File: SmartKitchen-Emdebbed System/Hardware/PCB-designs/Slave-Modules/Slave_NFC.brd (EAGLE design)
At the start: 90 x 80 mm, 29 parts, among them IC1 PCF8574T, IC2 7805DT, IC3 PCF8574T, IC4 74AHC1G126DBV, J1 RJ11-2L-B, J2 RJ11-2L-B, Q1 SPB80P06P, Q2 SPB80P06P, Q3 SPB80P06P

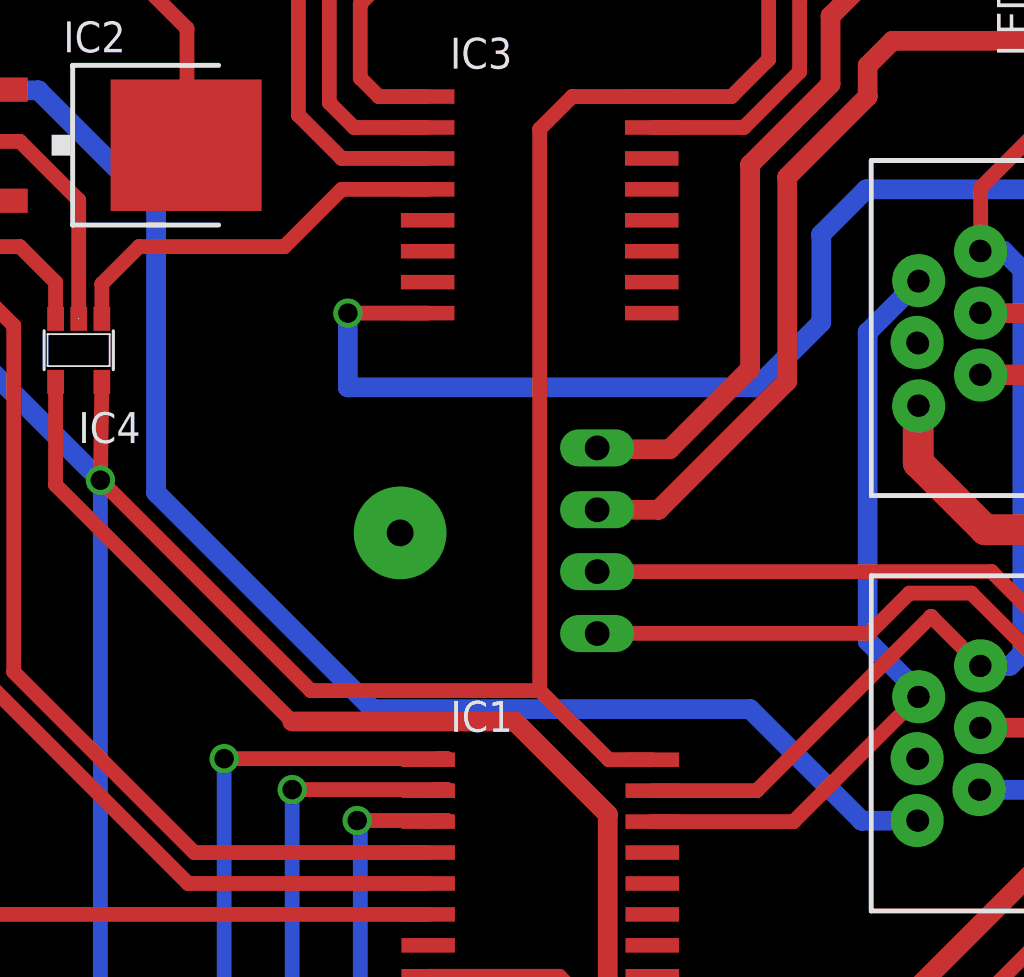
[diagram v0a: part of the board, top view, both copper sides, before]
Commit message: Testsoftware + Fix problem wire
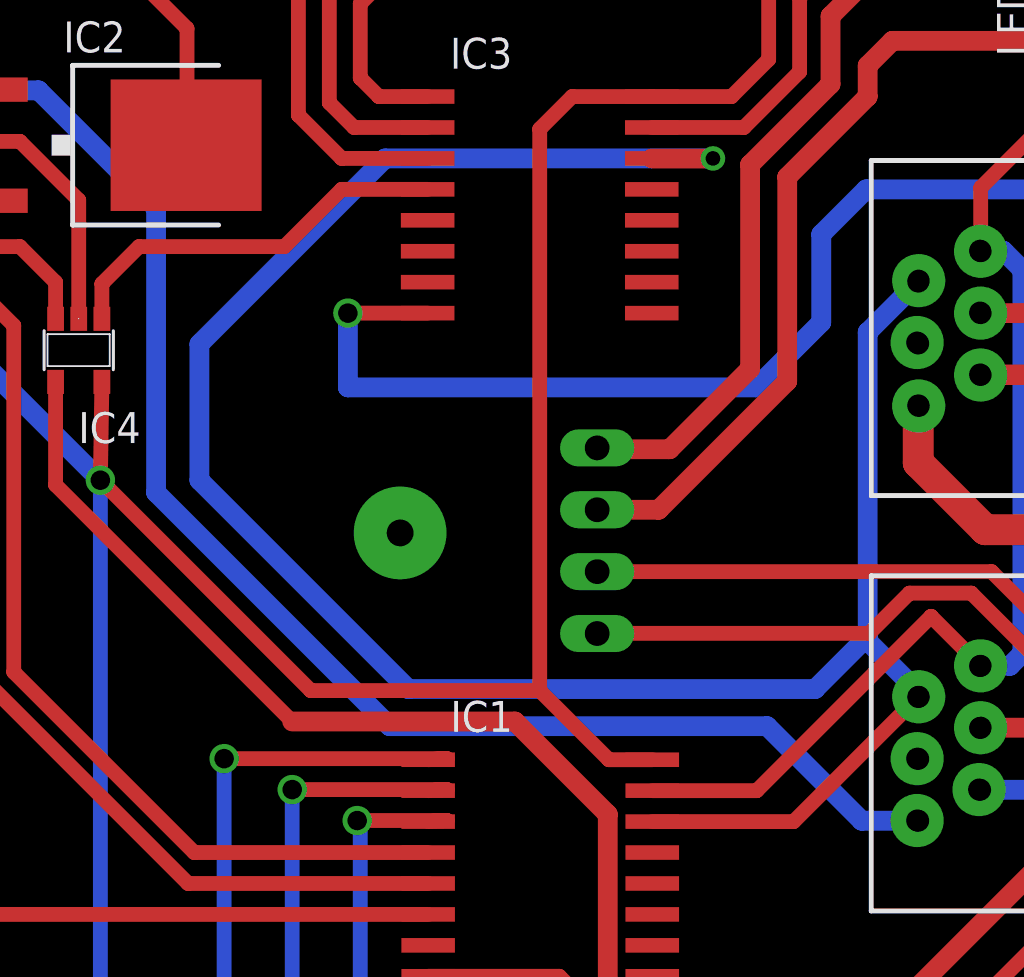
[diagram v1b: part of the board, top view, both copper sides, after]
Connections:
- net N$3: now also IC3.14
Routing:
- net N$3: track 31.8 -> 96.0 mm, vias 0 -> 1
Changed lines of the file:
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@@
 <wire x1="66.523" y1="76.225" x2="66.548" y2="76.2" width="1.27" layer="16"/>
 <wire x1="74.72" y1="28.185" x2="72.399" y2="28.185" width="0.8128" layer="16"/>
-<wire x1="72.399" y1="28.185" x2="67.818" y2="32.766" width="0.8128" layer="16"/>
-<wire x1="67.818" y1="32.766" x2="52.324" y2="32.766" width="0.8128" layer="16"/>
-<wire x1="52.324" y1="32.766" x2="43.434" y2="41.656" width="0.8128" layer="16"/>
+<wire x1="53.0225" y1="32.0675" x2="43.434" y2="41.656" width="0.8128" layer="16"/>
 <wire x1="43.434" y1="41.656" x2="43.434" y2="53.34" width="0.8128" layer="16"/>
 <wire x1="43.434" y1="53.34" x2="38.608" y2="58.166" width="0.8128" layer="16"/>
 <wire x1="38.608" y1="58.166" x2="35.306" y2="58.166" width="0.8128" layer="16"/>
 <wire x1="35.335" y1="58.195" x2="37.3675" y2="58.195" width="0.6096" layer="1"/>
+<wire x1="53.0225" y1="32.0675" x2="68.5165" y2="32.0675" width="0.8128" layer="16"/>
+<wire x1="68.5165" y1="32.0675" x2="72.399" y2="28.185" width="0.8128" layer="16"/>
 </signal>
 <signal name="N$1">
@@
 <wire x1="74.72" y1="33.265" x2="74.72" y2="33.484" width="0.8128" layer="16"/>
 <wire x1="74.72" y1="33.484" x2="72.644" y2="35.56" width="0.8128" layer="16"/>
-<wire x1="72.644" y1="35.56" x2="72.644" y2="48.239" width="0.8128" layer="16"/>
+<wire x1="72.644" y1="35.56" x2="72.644" y2="35.7505" width="0.8128" layer="16"/>
 <wire x1="72.644" y1="48.239" x2="74.72" y2="50.315" width="0.8128" layer="16"/>
 <wire x1="63.8025" y1="28.15" x2="69.605" y2="28.15" width="0.6096" layer="1"/>
 <wire x1="69.605" y1="28.15" x2="74.72" y2="33.265" width="0.6096" layer="1"/>
+<contactref element="IC3" pad="14"/>
+<wire x1="72.644" y1="48.239" x2="72.644" y2="35.7505" width="0.8128" layer="16"/>
+<wire x1="72.644" y1="35.7505" x2="70.485" y2="33.5915" width="0.8128" layer="16"/>
+<wire x1="70.485" y1="33.5915" x2="53.7845" y2="33.5915" width="0.8128" layer="16"/>
+<wire x1="53.7845" y1="33.5915" x2="45.212" y2="42.164" width="0.8128" layer="16"/>
+<wire x1="45.212" y1="42.164" x2="45.212" y2="47.752" width="0.8128" layer="16"/>
+<wire x1="45.212" y1="47.752" x2="52.832" y2="55.372" width="0.8128" layer="16"/>
+<wire x1="52.832" y1="55.372" x2="66.294" y2="55.372" width="0.8128" layer="16"/>
+<via x="66.294" y="55.372" extent="1-16" drill="0.6" shape="square"/>
+<wire x1="66.294" y1="55.372" x2="63.782" y2="55.372" width="0.8128" layer="1"/>
 </signal>
 <signal name="N$21">

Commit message: Optimized PCB-board 2.0 with header for MAX232
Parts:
- added X1: 22-23-2101, con-molex:22-23-2101
- moved INDILED 10.0 mm to (71.5, 39.7)
- moved R6 10.0 mm to (39.5, 24.3)
- moved IC1 10.0 mm to (69.2, 26.2)
- moved IC2 10.0 mm to (52.2, 55.9)
- moved IC3 10.0 mm to (69.2, 53.5)
- moved IC4 10.0 mm to (50.3, 47.5)
- moved J1 10.0 mm to (93.6, 48.4)
- moved J2 10.0 mm to (93.6, 31.4)
- moved LED1 10.0 mm to (91.0, 18.4)
- moved LED2 10.0 mm to (91.5, 61.5)
- moved Q1 10.0 mm to (28.6, 51.1)
- moved Q2 10.0 mm to (28.6, 37.7)
- moved Q3 10.0 mm to (28.6, 24.2)
- moved R1 10.0 mm to (43.7, 50.5)
- moved R10 10.0 mm to (82.6, 69.8)
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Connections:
- removed net N$27: IC4.2, SV1.5
- new net N$26: IC4.2, X1.2
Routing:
- net N$26: track 0.00 -> 91.0 mm, vias 0 -> 1
- net N$27: track 44.9 -> 0.00 mm
- net N$7: track 200.6 -> 231.9 mm
- net N$8: track 225.7 -> 222.5 mm
- net N$9: track 202.0 -> 200.5 mm
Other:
- board size 90 x 80 mm -> 100 x 80 mm
- board text added: "OAMK Design by Tom Mampaey Made in Finland"
- board text added: "Smart Fridge - OAMK"

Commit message: Adding interference capacitors and testingcode
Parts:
- added C1, C2: 100nF, rcl:C0603
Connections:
- net AGND: now also C1.1, C2.1
- net N$21: now also C1.2, C2.2
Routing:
- net AGND: track 311.1 -> 331.6 mm, vias 6 -> 7
- net N$21: track 224.4 -> 230.0 mm
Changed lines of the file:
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@@
 <setting verticaltext="up"/>
 </settings>
-<grid distance="0.02" unitdist="inch" unit="inch" style="lines" multiple="1" display="yes" altdistance="0.05" altunitdist="inch" altunit="inch"/>
+<grid distance="0.01" unitdist="inch" unit="inch" style="lines" multiple="1" display="yes" altdistance="0.05" altunitdist="inch" altunit="inch"/>
 <layers>
 <layer number="1" name="Top" color="4" fill="1" visible="yes" active="yes"/>
@@
 <attribute name="OC_FARNELL" value="1756828" x="11.2827" y="39.3733" size="1.778" layer="27" rot="R90" display="off"/>
 </element>
+<element name="C1" library="rcl" package="C0603" value="100nF" x="76.2" y="60.452" rot="R270"/>
+<element name="C2" library="rcl" package="C0603" value="100nF" x="76.2" y="33.02" rot="R270"/>
 </elements>
 <signals>
@@
 <via x="90.518" y="46.482" extent="1-16" drill="0.8" shape="square"/>
 <wire x1="90.518" y1="46.482" x2="87.283" y2="46.482" width="0.8128" layer="1"/>
-<wire x1="87.26" y1="29.455" x2="90.509" y2="29.455" width="0.8128" layer="16"/>
+<wire x1="87.26" y1="29.455" x2="89.154" y2="29.455" width="0.8128" layer="16"/>
+<wire x1="89.154" y1="29.455" x2="90.509" y2="29.455" width="0.8128" layer="16"/>
 <wire x1="90.509" y1="29.455" x2="90.518" y2="29.464" width="0.8128" layer="16"/>
 <wire x1="90.495" y1="46.505" x2="90.518" y2="46.482" width="0.8128" layer="16"/>
@@
 <via x="43.274" y="51.7525" extent="1-16" drill="0.6" shape="square"/>
 <wire x1="64.582" y1="49.022" x2="61.308" y2="49.022" width="0.6096" layer="1"/>
+<contactref element="C1" pad="1"/>
+<contactref element="C2" pad="1"/>
+<wire x1="76.2" y1="33.87" x2="77.47" y2="33.87" width="0.6096" layer="1"/>
+<wire x1="77.47" y1="33.87" x2="77.47" y2="30.734" width="0.6096" layer="1"/>
+<via x="77.47" y="30.734" extent="1-16" drill="0.6" shape="square"/>
+<wire x1="77.47" y1="30.734" x2="77.724" y2="30.48" width="0.6096" layer="16"/>
+<wire x1="77.724" y1="30.48" x2="78.232" y2="30.48" width="0.6096" layer="16"/>
+<wire x1="78.232" y1="30.48" x2="83.566" y2="25.146" width="0.6096" layer="16"/>
+<wire x1="83.566" y1="25.146" x2="85.344" y2="25.146" width="0.6096" layer="16"/>
+<wire x1="85.344" y1="25.146" x2="89.154" y2="28.956" width="0.6096" layer="16"/>
+<wire x1="89.154" y1="28.956" x2="89.154" y2="29.455" width="0.6096" layer="16"/>
 </signal>
 <signal name="N$4">
@@
 <wire x1="78.58" y1="62.484" x2="78.58" y2="59.436" width="0.6096" layer="1"/>
 <wire x1="78.58" y1="59.436" x2="77.056" y2="57.912" width="0.6096" layer="1"/>
-<wire x1="77.056" y1="57.912" x2="73.782" y2="57.912" width="0.6096" layer="1"/>
+<wire x1="77.056" y1="57.912" x2="76.2" y2="57.912" width="0.6096" layer="1"/>
+<wire x1="76.2" y1="57.912" x2="73.782" y2="57.912" width="0.6096" layer="1"/>
 <wire x1="95.4583" y1="5.715" x2="95.4583" y2="8.255" width="0.8128" layer="1"/>
 <wire x1="95.4583" y1="8.255" x2="95.4583" y2="10.795" width="0.8128" layer="1"/>
@@
 <wire x1="70.5155" y1="57.912" x2="69.182" y2="56.5785" width="0.6096" layer="1"/>
 <wire x1="69.182" y1="56.5785" x2="69.182" y2="33.528" width="0.6096" layer="1"/>
+<contactref element="C1" pad="2"/>
+<wire x1="76.2" y1="59.602" x2="76.2" y2="57.912" width="0.4064" layer="1"/>
+<contactref element="C2" pad="2"/>
+<wire x1="76.2" y1="32.17" x2="76.2" y2="30.734" width="0.6096" layer="1"/>
+<wire x1="76.2" y1="30.734" x2="73.8025" y2="30.734" width="0.6096" layer="1"/>
+<wire x1="73.8025" y1="30.734" x2="73.8025" y2="30.69" width="0.6096" layer="1"/>
 <wire x1="51.2115" y1="46.2005" x2="51.209" y2="46.198" width="0" layer="19" extent="1-1"/>
 </signal>

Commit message: Final PCB-design for NFC-reader modules
I'm proud
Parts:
- added C3, C4: 100n, resistor:C0603
- C1, C2: value 100nF -> 4µ7; device rcl:C0603 -> resistor:PANASONIC_B
- moved C1 36.7 mm to (79.2, 23.9), turned to 0 degrees
- moved C2 8.68 mm to (79.2, 41.1), turned to 0 degrees
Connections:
- net AGND: now also C1.-, C2.-, C3.1, C4.1; no longer C1.1, C2.1
- net N$10: now also C1.+, C2.+, J1.3, J2.3
- net N$21: now also C3.2, C4.2; no longer C1.2, C2.2
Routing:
- net AGND: track 331.6 -> 311.1 mm, vias 7 -> 27
- net N$10: track 338.7 -> 356.7 mm
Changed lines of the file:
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@@
 <setting verticaltext="up"/>
 </settings>
-<grid distance="0.01" unitdist="inch" unit="inch" style="lines" multiple="1" display="yes" altdistance="0.05" altunitdist="inch" altunit="inch"/>
+<grid distance="0.00125" unitdist="inch" unit="inch" style="lines" multiple="1" display="yes" altdistance="0.05" altunitdist="inch" altunit="inch"/>
 <layers>
 <layer number="1" name="Top" color="4" fill="1" visible="yes" active="yes"/>
@@
 <wire x1="80" y1="62.5" x2="80" y2="17.5" width="0.4064" layer="22" style="longdash"/>
 <wire x1="10" y1="62.5" x2="10" y2="17.5" width="0.4064" layer="22" style="longdash"/>
-<text x="7.62" y="30.988" size="2.54" layer="1" ratio="24" rot="SR270" align="top-center">Smart Fridge - OAMK</text>
+<text x="7.20725" y="31.1785" size="2.54" layer="1" ratio="24" rot="SR270" align="top-center">Smart Fridge - OAMK</text>
 <text x="34.544" y="37.592" size="3.048" layer="16" ratio="24" rot="SMR90" align="top-center">OAMK
 Design by
@@
 <attribute name="OC_FARNELL" value="1756828" x="11.2827" y="39.3733" size="1.778" layer="27" rot="R90" display="off"/>
 </element>
-<element name="C1" library="rcl" package="C0603" value="100nF" x="76.2" y="60.452" rot="R270"/>
-<element name="C2" library="rcl" package="C0603" value="100nF" x="76.2" y="33.02" rot="R270"/>
+<element name="C1" library="resistor" package="PANASONIC_B" value="4µ7" x="79.248" y="23.876"/>
+<element name="C2" library="resistor" package="PANASONIC_B" value="4µ7" x="79.248" y="41.148"/>
+<element name="C3" library="resistor" package="C0603" value="100n" x="75.565" y="60.452" rot="R270"/>
+<element name="C4" library="resistor" package="C0603" value="100n" x="76.073" y="33.02" rot="R270"/>
 </elements>
 <signals>
@@
 <via x="90.518" y="46.482" extent="1-16" drill="0.8" shape="square"/>
 <wire x1="90.518" y1="46.482" x2="87.283" y2="46.482" width="0.8128" layer="1"/>
-<wire x1="87.26" y1="29.455" x2="89.154" y2="29.455" width="0.8128" layer="16"/>
-<wire x1="89.154" y1="29.455" x2="90.509" y2="29.455" width="0.8128" layer="16"/>
+<wire x1="87.26" y1="29.455" x2="90.509" y2="29.455" width="0.8128" layer="16"/>
 <wire x1="90.509" y1="29.455" x2="90.518" y2="29.464" width="0.8128" layer="16"/>
 <wire x1="90.495" y1="46.505" x2="90.518" y2="46.482" width="0.8128" layer="16"/>
@@
 <via x="43.274" y="51.7525" extent="1-16" drill="0.6" shape="square"/>
 <wire x1="64.582" y1="49.022" x2="61.308" y2="49.022" width="0.6096" layer="1"/>
-<contactref element="C1" pad="1"/>
-<contactref element="C2" pad="1"/>
-<wire x1="76.2" y1="33.87" x2="77.47" y2="33.87" width="0.6096" layer="1"/>
-<wire x1="77.47" y1="33.87" x2="77.47" y2="30.734" width="0.6096" layer="1"/>
-<via x="77.47" y="30.734" extent="1-16" drill="0.6" shape="square"/>
-<wire x1="77.47" y1="30.734" x2="77.724" y2="30.48" width="0.6096" layer="16"/>
-<wire x1="77.724" y1="30.48" x2="78.232" y2="30.48" width="0.6096" layer="16"/>
-<wire x1="78.232" y1="30.48" x2="83.566" y2="25.146" width="0.6096" layer="16"/>
-<wire x1="83.566" y1="25.146" x2="85.344" y2="25.146" width="0.6096" layer="16"/>
-<wire x1="85.344" y1="25.146" x2="89.154" y2="28.956" width="0.6096" layer="16"/>
-<wire x1="89.154" y1="28.956" x2="89.154" y2="29.455" width="0.6096" layer="16"/>
+<contactref element="C4" pad="1"/>
+<contactref element="C2" pad="-"/>
+<contactref element="C1" pad="-"/>
+<contactref element="C3" pad="1"/>
+<via x="22.606" y="16.256" extent="1-16" drill="0.6" shape="square"/>
+<via x="12.192" y="3.429" extent="1-16" drill="0.6" shape="square"/>
+<via x="48.133" y="16.383" extent="1-16" drill="0.6" shape="square"/>
+<via x="45.847" y="28.448" extent="1-16" drill="0.6" shape="square"/>
+<via x="53.34" y="32.893" extent="1-16" drill="0.6" shape="square"/>
+<via x="84.836" y="56.769" extent="1-16" drill="0.6" shape="square"/>
+<via x="76.327" y="49.403" extent="1-16" drill="0.6" shape="square"/>
+<via x="10.541" y="68.707" extent="1-16" drill="0.6" shape="square"/>
+<via x="15.24" y="76.962" extent="1-16" drill="0.6" shape="square"/>
+<via x="95.504" y="14.859" extent="1-16" drill="0.6" shape="square"/>
+<via x="52.705" y="63.754" extent="1-16" drill="0.6" shape="square"/>
+<via x="10.541" y="17.907" extent="1-16" drill="0.6" shape="square"/>
+<via x="84.709" y="16.256" extent="1-16" drill="0.6" shape="square"/>
+<via x="70.993" y="51.689" extent="1-16" drill="0.6" shape="square"/>
+<via x="4.064" y="56.134" extent="1-16" drill="0.6" shape="square"/>
+<via x="8.001" y="51.308" extent="1-16" drill="0.6" shape="square"/>
+<via x="81.534" y="21.463" extent="1-16" drill="0.6" shape="square"/>
+<via x="75.565" y="39.878" extent="1-16" drill="0.6" shape="square"/>
+<via x="77.47" y="30.6705" extent="1-16" drill="0.6" shape="square"/>
+<via x="77.69225" y="37.1475" extent="1-16" drill="0.6" shape="square"/>
+<via x="10.541" y="9.81075" extent="1-16" drill="0.6" shape="square"/>
 </signal>
 <signal name="N$4">
@@
 <wire x1="72.6475" y1="3.81" x2="72.6" y2="3.8575" width="1.27" layer="1"/>
 <wire x1="84.72" y1="45.235" x2="84.72" y2="42.882" width="1.27" layer="1"/>
-<wire x1="84.72" y1="42.882" x2="87.47" y2="40.132" width="1.27" layer="1"/>
+<wire x1="84.72" y1="42.882" x2="86.3435" y2="41.2585" width="1.27" layer="1"/>
+<wire x1="86.3435" y1="41.2585" x2="87.47" y2="40.132" width="1.27" layer="1"/>
 <wire x1="87.47" y1="40.132" x2="98.138" y2="40.132" width="1.27" layer="1"/>
 <via x="98.138" y="40.132" extent="1-16" drill="0.8" shape="square"/>
@@
 <wire x1="63.0225" y1="32.0675" x2="78.5165" y2="32.0675" width="0.8128" layer="16"/>
 <wire x1="78.5165" y1="32.0675" x2="82.399" y2="28.185" width="0.8128" layer="16"/>
+<contactref element="C2" pad="+"/>
+<contactref element="C1" pad="+"/>
+<contactref element="J1" pad="3"/>
+<contactref element="J2" pad="3"/>
+<wire x1="84.72" y1="28.185" x2="84.72" y2="30.725" width="1.27" layer="16"/>
+<wire x1="84.72" y1="47.775" x2="84.72" y2="45.235" width="1.27" layer="16"/>
+<wire x1="84.836" y1="28.069" x2="84.72" y2="28.185" width="0.8128" layer="1"/>
+<wire x1="80.848" y1="23.876" x2="83.058" y2="23.876" width="0.8128" layer="1"/>
+<wire x1="83.058" y1="23.876" x2="84.709" y2="25.527" width="0.8128" layer="1"/>
+<wire x1="84.709" y1="25.527" x2="84.709" y2="28.174" width="0.8128" layer="1"/>
+<wire x1="84.709" y1="28.174" x2="84.72" y2="28.185" width="0.8128" layer="1"/>
+<wire x1="80.848" y1="41.148" x2="86.3435" y2="41.148" width="0.8128" layer="1"/>
+<wire x1="86.3435" y1="41.148" x2="86.3435" y2="41.2585" width="0.8128" layer="1"/>
 </signal>
 <signal name="N$1">
@@
 <wire x1="78.58" y1="62.484" x2="78.58" y2="59.436" width="0.6096" layer="1"/>
 <wire x1="78.58" y1="59.436" x2="77.056" y2="57.912" width="0.6096" layer="1"/>
-<wire x1="77.056" y1="57.912" x2="76.2" y2="57.912" width="0.6096" layer="1"/>
-<wire x1="76.2" y1="57.912" x2="73.782" y2="57.912" width="0.6096" layer="1"/>
+<wire x1="77.056" y1="57.912" x2="75.565" y2="57.912" width="0.6096" layer="1"/>
+<wire x1="75.565" y1="57.912" x2="73.782" y2="57.912" width="0.6096" layer="1"/>
 <wire x1="95.4583" y1="5.715" x2="95.4583" y2="8.255" width="0.8128" layer="1"/>
 <wire x1="95.4583" y1="8.255" x2="95.4583" y2="10.795" width="0.8128" layer="1"/>
@@
 <wire x1="70.5155" y1="57.912" x2="69.182" y2="56.5785" width="0.6096" layer="1"/>
 <wire x1="69.182" y1="56.5785" x2="69.182" y2="33.528" width="0.6096" layer="1"/>
-<contactref element="C1" pad="2"/>
-<wire x1="76.2" y1="59.602" x2="76.2" y2="57.912" width="0.4064" layer="1"/>
-<contactref element="C2" pad="2"/>
-<wire x1="76.2" y1="32.17" x2="76.2" y2="30.734" width="0.6096" layer="1"/>
-<wire x1="76.2" y1="30.734" x2="73.8025" y2="30.734" width="0.6096" layer="1"/>
-<wire x1="73.8025" y1="30.734" x2="73.8025" y2="30.69" width="0.6096" layer="1"/>
+<contactref element="C4" pad="2"/>
+<contactref element="C3" pad="2"/>
+<wire x1="73.8025" y1="30.69" x2="76.073" y2="30.69" width="0.6096" layer="1"/>
+<wire x1="76.073" y1="30.69" x2="76.073" y2="32.17" width="0.6096" layer="1"/>
+<wire x1="75.565" y1="59.602" x2="75.565" y2="57.912" width="0.6096" layer="1"/>
 <wire x1="51.2115" y1="46.2005" x2="51.209" y2="46.198" width="0" layer="19" extent="1-1"/>
 </signal>
